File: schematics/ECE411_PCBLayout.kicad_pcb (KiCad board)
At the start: 2 copper layers, 88.9 x 63.5 mm, 3 parts

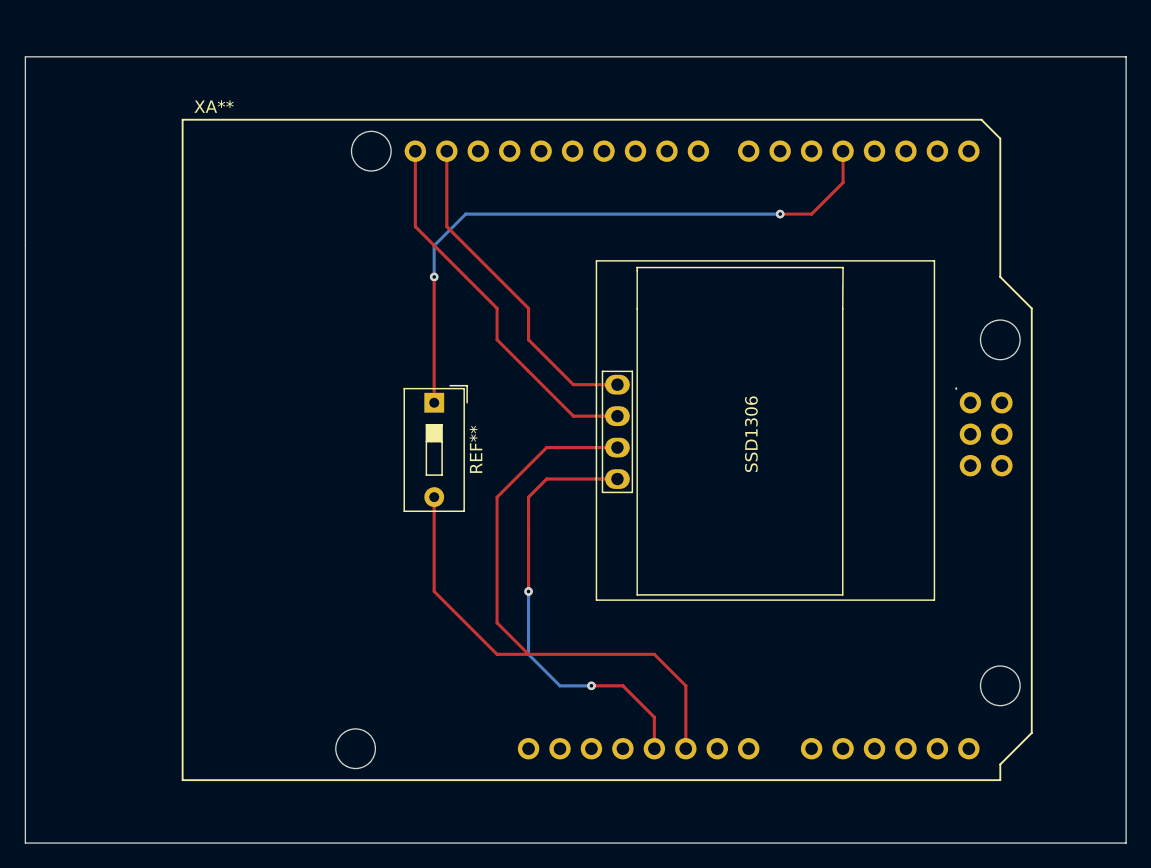
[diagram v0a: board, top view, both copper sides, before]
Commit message: updated pcb and circuit schematic
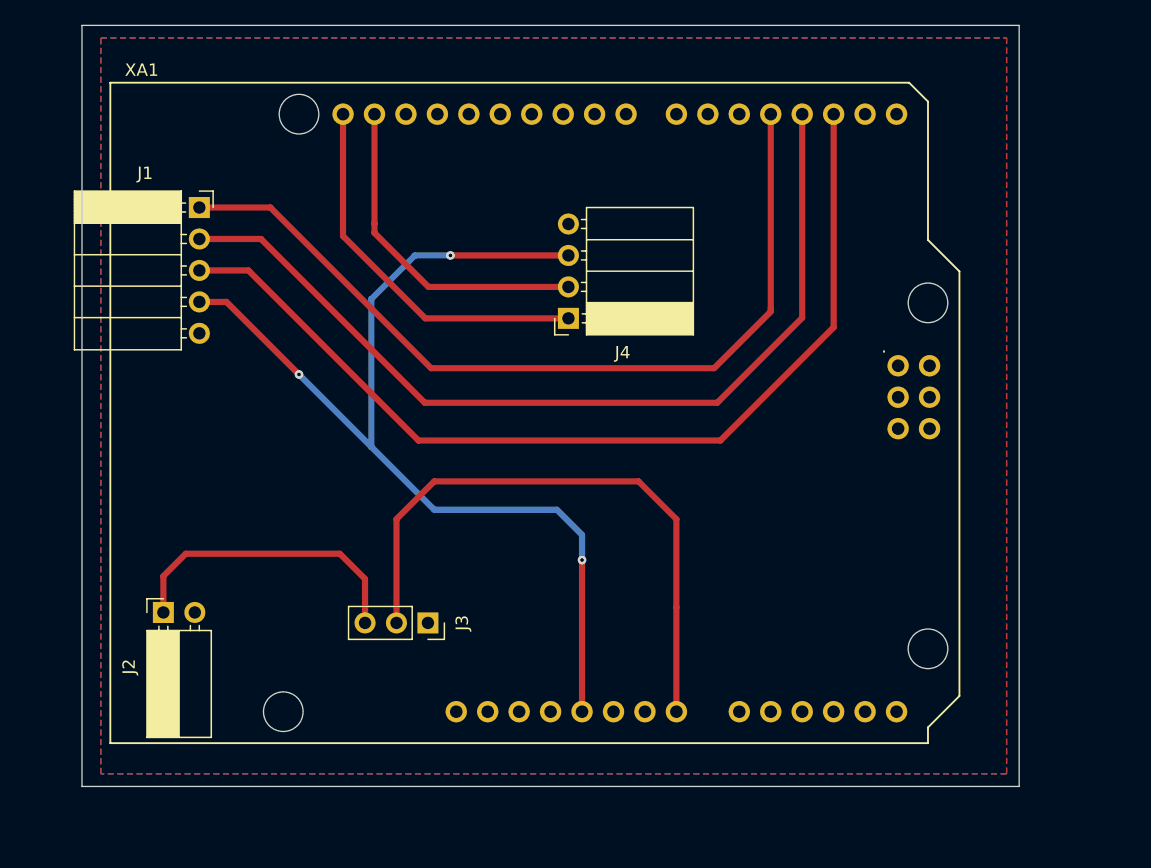
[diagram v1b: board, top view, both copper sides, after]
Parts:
- removed REF**: SW_DIP_SPSTx01_Slide_9.78x4.72mm_W7.62mm_P2.54mm, Button_Switch_THT:SW_DIP_SPSTx01_Slide_9.78x4.72mm_W7.62mm_P2.54mm
- removed SSD1306: 128x64OLED, SSD1306:128x64OLED
- removed XA**: Arduino_Uno_Shield, Arduino:Arduino_Uno_Shield
- added J1: Rotary Encoder, Connector_PinSocket_2.54mm:PinSocket_1x05_P2.54mm_Horizontal, F.Cu at (115.7, 68.1)
- added J2: Power, Connector_PinSocket_2.54mm:PinSocket_1x02_P2.54mm_Horizontal, F.Cu at (112.7, 100.8)
- added J3: Switch, Connector_PinSocket_2.54mm:PinSocket_1x03_P2.54mm_Vertical, F.Cu at (134.1, 101.6)
- added J4: LCD_I2C, Connector_PinSocket_2.54mm:PinSocket_1x04_P2.54mm_Horizontal, F.Cu at (145.5, 77.0)
- added XA1: Arduino_Uno_Shield, Arduino:Arduino_Uno_Shield, F.Cu at (108.5, 111.3)
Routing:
- net (no net): track 203.9 -> 0.00 mm, vias 4 -> 0
- net Net-(J1-Pad4): track 0.00 -> 82.3 mm, vias 0 -> 3
- net Net-(J1-Pad3): track 0.00 -> 77.9 mm
- net Net-(J1-Pad2): track 0.00 -> 73.5 mm
- net Net-(J1-Pad1): track 0.00 -> 69.4 mm
- net Net-(J3-Pad2): track 0.00 -> 49.1 mm
- net Net-(J4-Pad1): track 0.00 -> 30.8 mm
- net Net-(J4-Pad2): track 0.00 -> 27.1 mm
- net Net-(J2-Pad1): track 0.00 -> 24.4 mm
- added copper zone on B.Cu, net GND
- added copper zone on F.Cu, net GND
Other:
- board size 88.9 x 63.5 mm -> 75.7 x 61.5 mm
- rule pad_to_mask_clearance: 0.05 -> 0

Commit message: final CAD
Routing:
- net Net-(J1-Pad4): vias 3 -> 0
- net GND: vias 0 -> 18
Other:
- board text added: "ECE 411 Team 3 2022/11/15 V1 Alex Kim Celina Wang Dmytro Prystupa Huibo Yu"
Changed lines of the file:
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@@
   )
   (gr_rect (start 106.172 53.34) (end 181.864 114.808) (layer "Edge.Cuts") (width 0.1) (fill none))
-  (segment (start 115.652 75.672) (end 117.836 75.672) (width 0.5) (layer "F.Cu") (net 2))
-  (segment (start 146.56 96.522) (end 146.56 108.77) (width 0.5) (layer "F.Cu") (net 2))
-  (segment (start 146.558 96.52) (end 146.56 96.522) (width 0.5) (layer "F.Cu") (net 2))
-  (segment (start 145.46 71.922) (end 135.93 71.922) (width 0.5) (layer "F.Cu") (net 2))
-  (segment (start 117.836 75.672) (end 123.698 81.534) (width 0.5) (layer "F.Cu") (net 2))
-  (via (at 135.93 71.922) (size 0.7) (drill 0.3) (layers "F.Cu" "B.Cu") (net 2))
-  (via (at 123.698 81.534) (size 0.7) (drill 0.3) (layers "F.Cu" "B.Cu") (net 2))
-  (via (at 146.558 96.52) (size 0.7) (drill 0.3) (layers "F.Cu" "B.Cu") (net 2))
-  (segment (start 133.056 71.922) (end 129.54 75.438) (width 0.5) (layer "B.Cu") (net 2))
-  (segment (start 135.93 71.922) (end 133.056 71.922) (width 0.5) (layer "B.Cu") (net 2))
-  (segment (start 123.698 81.534) (end 129.54 87.376) (width 0.5) (layer "B.Cu") (net 2))
+  (gr_text "ECE 411 Team 3 2022/11/15 V1\nAlex Kim\nCelina Wang\nDmytro Prystupa\nHuibo Yu" (at 157.226 94.234) (layer "F.SilkS")
+    (effects (font (size 1.5 1.5) (thickness 0.3)))
+  )
+  (via (at 122.428 102.87) (size 0.7) (drill 0.3) (layers "F.Cu" "B.Cu") (free) (net 1))
+  (via (at 159.004 65.024) (size 0.7) (drill 0.3) (layers "F.Cu" "B.Cu") (free) (net 1))
+  (via (at 122.936 78.486) (size 0.7) (drill 0.3) (layers "F.Cu" "B.Cu") (free) (net 1))
+  (via (at 158.496 75.692) (size 0.7) (drill 0.3) (layers "F.Cu" "B.Cu") (free) (net 1))
+  (via (at 168.656 91.186) (size 0.7) (drill 0.3) (layers "F.Cu" "B.Cu") (free) (net 1))
+  (via (at 171.704 65.278) (size 0.7) (drill 0.3) (layers "F.Cu" "B.Cu") (free) (net 1))
+  (via (at 142.748 104.14) (size 0.7) (drill 0.3) (layers "F.Cu" "B.Cu") (free) (net 1))
+  (via (at 134.366 93.726) (size 0.7) (drill 0.3) (layers "F.Cu" "B.Cu") (free) (net 1))
+  (via (at 147.066 92.202) (size 0.7) (drill 0.3) (layers "F.Cu" "B.Cu") (free) (net 1))
+  (via (at 112.268 84.074) (size 0.7) (drill 0.3) (layers "F.Cu" "B.Cu") (free) (net 1))
+  (via (at 170.688 76.454) (size 0.7) (drill 0.3) (layers "F.Cu" "B.Cu") (free) (net 1))
+  (via (at 150.876 104.14) (size 0.7) (drill 0.3) (layers "F.Cu" "B.Cu") (free) (net 1))
+  (via (at 165.1 104.394) (size 0.7) (drill 0.3) (layers "F.Cu" "B.Cu") (free) (net 1))
+  (via (at 136.652 64.77) (size 0.7) (drill 0.3) (layers "F.Cu" "B.Cu") (free) (net 1))
+  (via (at 156.972 91.44) (size 0.7) (drill 0.3) (layers "F.Cu" "B.Cu") (free) (net 1))
+  (via (at 122.682 92.71) (size 0.7) (drill 0.3) (layers "F.Cu" "B.Cu") (free) (net 1))
+  (via (at 148.59 64.77) (size 0.7) (drill 0.3) (layers "F.Cu" "B.Cu") (free) (net 1))
+  (via (at 121.412 65.024) (size 0.7) (drill 0.3) (layers "F.Cu" "B.Cu") (free) (net 1))
+  (segment (start 146.558 96.52) (end 146.56 96.522) (width 0.5) (layer "B.Cu") (net 2))
+  (segment (start 117.836 75.672) (end 115.652 75.672) (width 0.5) (layer "B.Cu") (net 2))
+  (segment (start 129.54 75.438) (end 133.056 71.922) (width 0.5) (layer "B.Cu") (net 2))
+  (segment (start 133.056 71.922) (end 145.46 71.922) (width 0.5) (layer "B.Cu") (net 2))
+  (segment (start 129.54 87.376) (end 117.836 75.672) (width 0.5) (layer "B.Cu") (net 2))
   (segment (start 146.558 94.488) (end 146.558 96.52) (width 0.5) (layer "B.Cu") (net 2))
-  (segment (start 129.54 75.438) (end 129.54 87.376) (width 0.5) (layer "B.Cu") (net 2))
   (segment (start 144.526 92.456) (end 146.558 94.488) (width 0.5) (layer "B.Cu") (net 2))
+  (segment (start 146.56 96.522) (end 146.56 108.77) (width 0.5) (layer "B.Cu") (net 2))
+  (segment (start 129.54 87.376) (end 129.54 75.438) (width 0.5) (layer "B.Cu") (net 2))
   (segment (start 129.54 87.376) (end 134.62 92.456) (width 0.5) (layer "B.Cu") (net 2))
   (segment (start 134.62 92.456) (end 144.526 92.456) (width 0.5) (layer "B.Cu") (net 2))

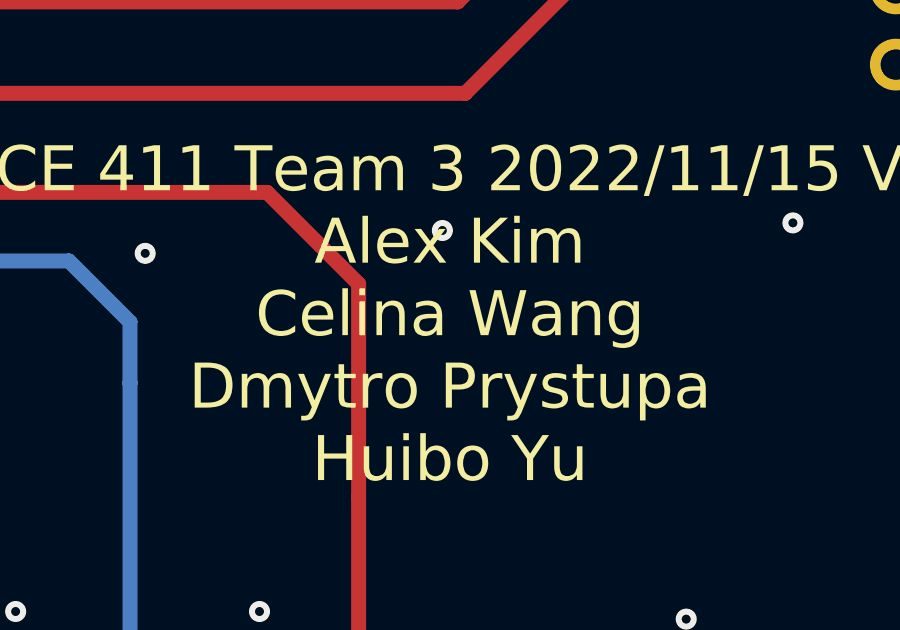
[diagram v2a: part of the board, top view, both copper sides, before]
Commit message: fixed name typo
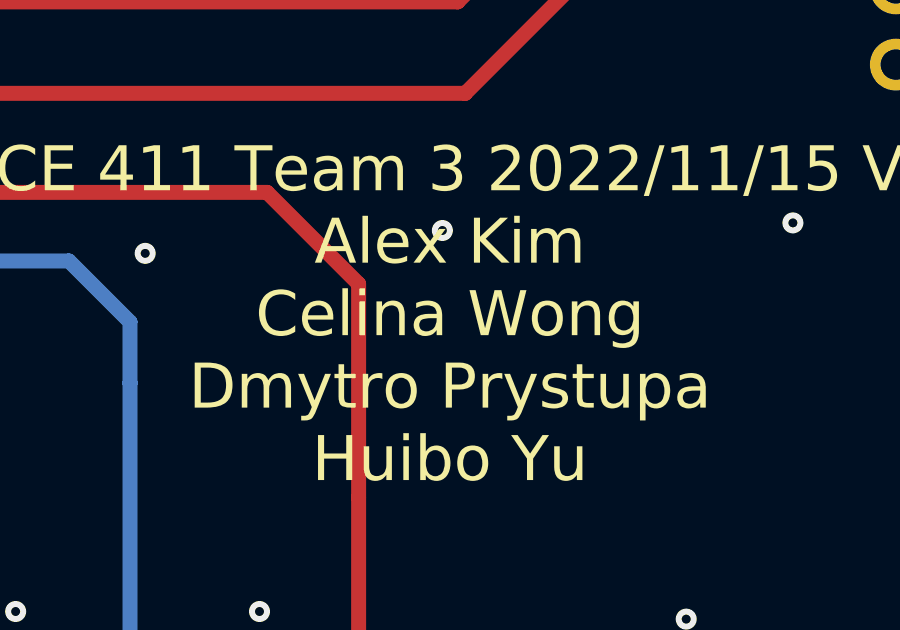
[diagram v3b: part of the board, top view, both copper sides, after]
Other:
- board text added: "ECE 411 Team 3 2022/11/15 V1 Alex Kim Celina Wong Dmytro Prystupa Huibo Yu"
- board text removed: "ECE 411 Team 3 2022/11/15 V1 Alex Kim Celina Wang Dmytro Prystupa Huibo Yu"
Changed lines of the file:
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@@
   )
   (gr_rect (start 106.172 53.34) (end 181.864 114.808) (layer "Edge.Cuts") (width 0.1) (fill none))
-  (gr_text "ECE 411 Team 3 2022/11/15 V1\nAlex Kim\nCelina Wang\nDmytro Prystupa\nHuibo Yu" (at 157.226 94.234) (layer "F.SilkS")
+  (gr_text "ECE 411 Team 3 2022/11/15 V1\nAlex Kim\nCelina Wong\nDmytro Prystupa\nHuibo Yu" (at 157.226 94.234) (layer "F.SilkS")
     (effects (font (size 1.5 1.5) (thickness 0.3)))
   )
